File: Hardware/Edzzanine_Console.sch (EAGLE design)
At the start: 37 parts, among them U2 FTS31XS-U, U4 TPS62065

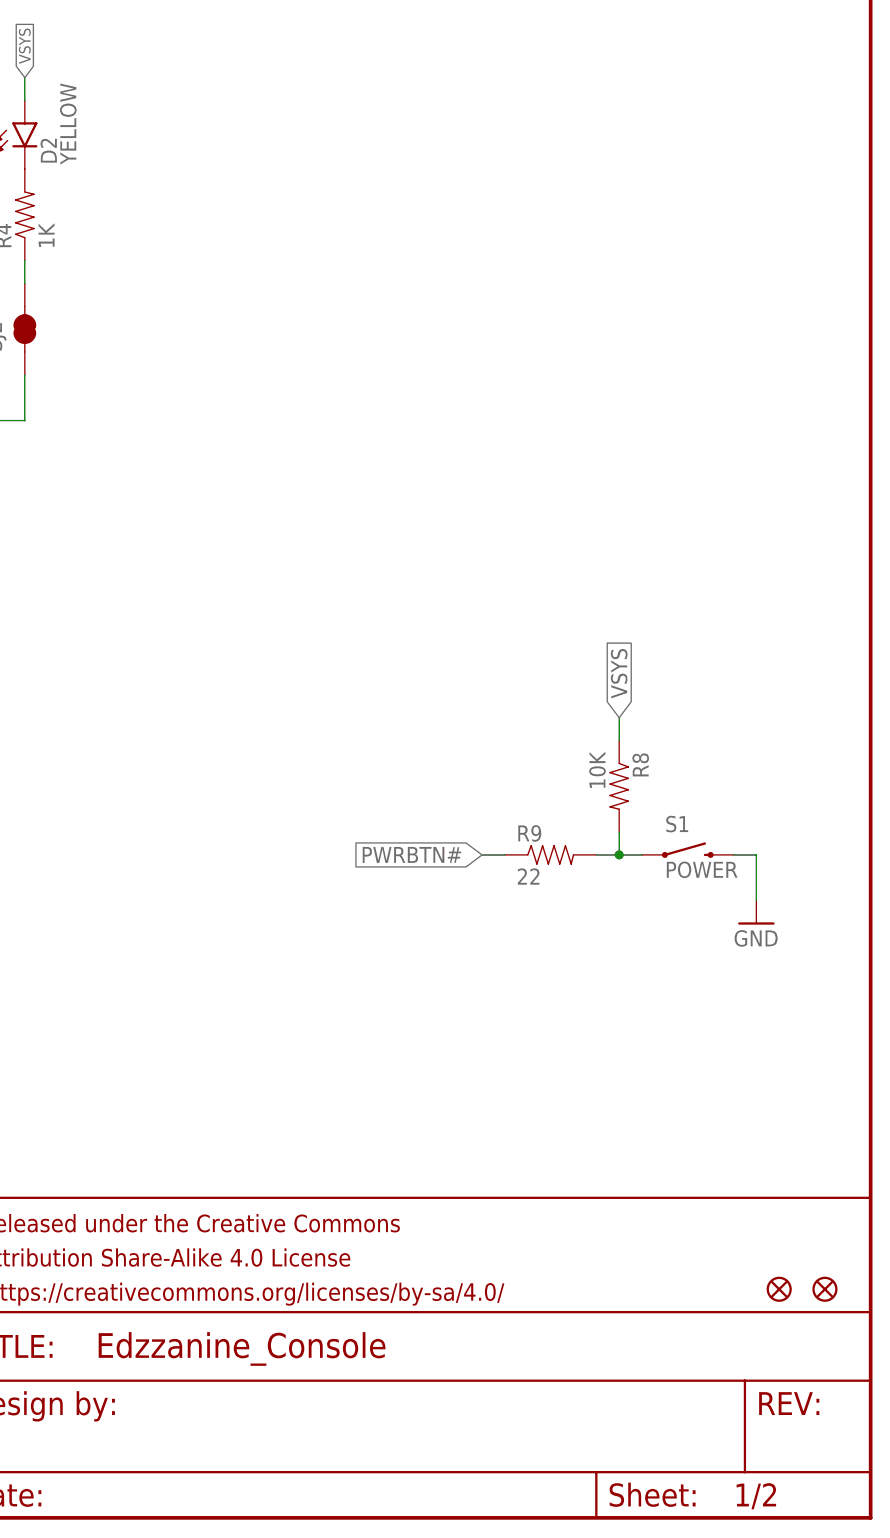
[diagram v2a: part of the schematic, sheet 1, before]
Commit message: Added DCIN enable circuit replaced power button with new side shooting SMD switch Fixed dimensions corrected ground planes to not include orphans corrected name of board added DCIN pin
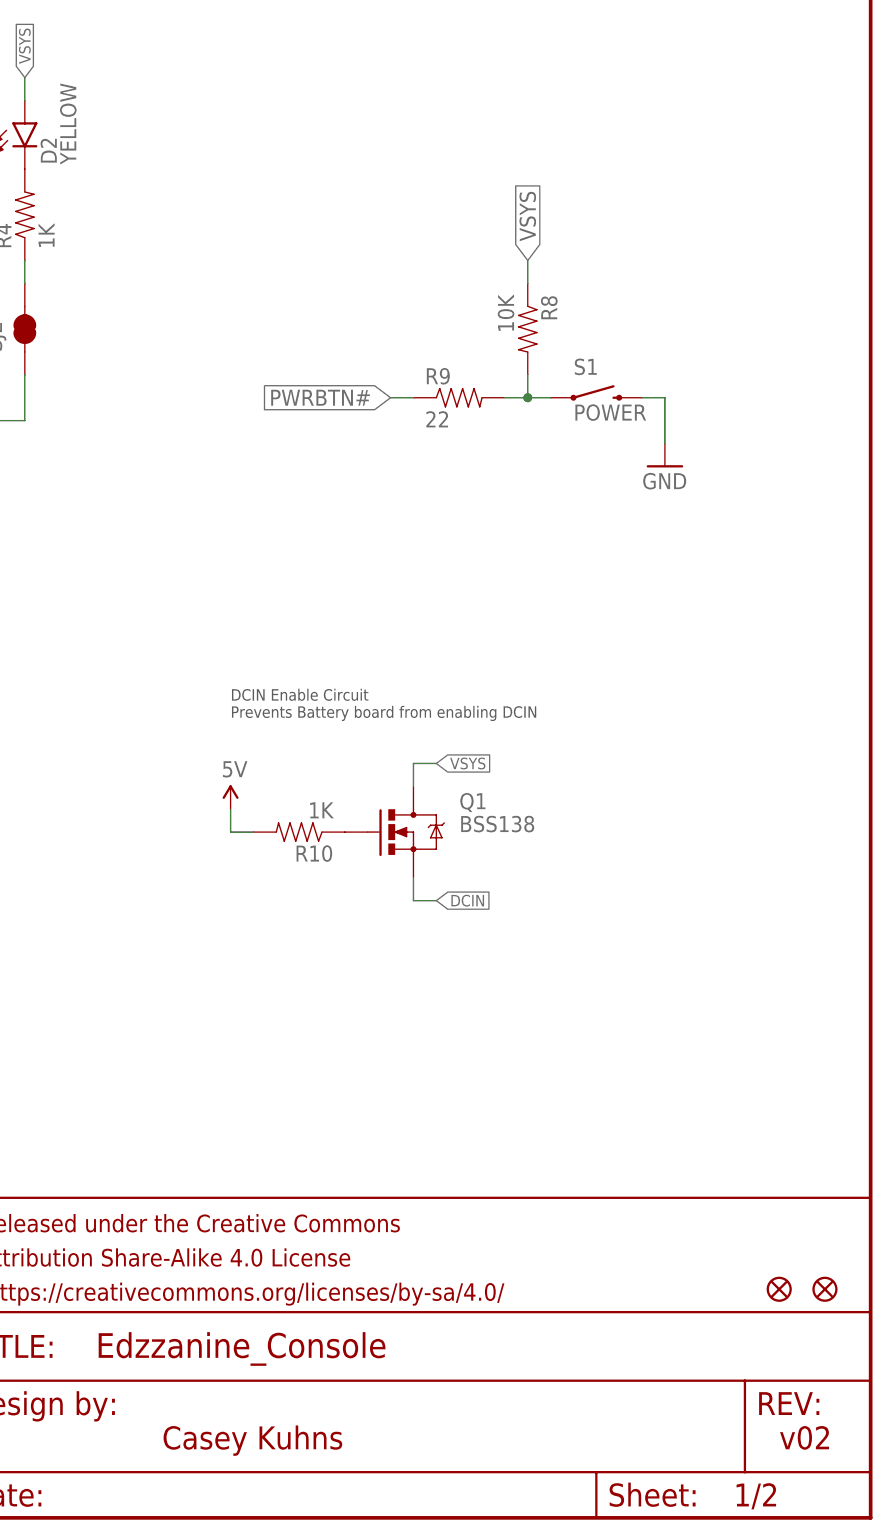
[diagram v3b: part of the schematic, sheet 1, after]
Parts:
- added Q1: BSS138, SparkFun-DiscreteSemi:MOSFET-NCHANNELBSS138
- added R10: 1K, SparkFun-Resistors:1KOHM1/10W1%(0603)
- S1: device SparkFun-Electromechanical:SWITCH-MOMENTARY-2-SMD-1101NE -> SparkFun-Electromechanical:SWITCH-MOMENTARY-2TACTILE-SWITCH-SMD-RIGHT-ANGLE
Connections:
- new net DCIN: E1.DCIN, Q1.S, U$3.DCIN
- new net N$16: Q1.G, R10.1
- net 5V: now also R10.2
- net VSYS: now also Q1.D
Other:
- note added: "Casey Kuhns"
- note added: "DCIN Enable Circuit Prevents Battery board from enabling DCIN"
- note added: "v02"
- moved on the sheet: R8, R9, S1
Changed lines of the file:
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@@
 <part name="R6" library="SparkFun-Resistors" deviceset="100OHM1/10W1%(0603)" device="" value="100"/>
 <part name="R7" library="SparkFun-Resistors" deviceset="100OHM1/10W1%(0603)" device="" value="100"/>
-<part name="S1" library="SparkFun-Electromechanical" deviceset="SWITCH-MOMENTARY-2" device="-SMD-1101NE" value="POWER"/>
+<part name="S1" library="SparkFun-Electromechanical" deviceset="SWITCH-MOMENTARY-2" device="TACTILE-SWITCH-SMD-RIGHT-ANGLE" value="POWER"/>
 <part name="R8" library="SparkFun-Resistors" deviceset="10KOHM1/10W1%(0603)" device="0603" value="10K"/>
 <part name="R9" library="SparkFun-Resistors" deviceset="22OHM1/10W1%(0603)" device="" value="22"/>
@@
 <part name="FID1" library="SparkFun-Aesthetics" deviceset="FIDUCIAL" device="1X2"/>
 <part name="FID2" library="SparkFun-Aesthetics" deviceset="FIDUCIAL" device="1X2"/>
+<part name="Q1" library="SparkFun-DiscreteSemi" deviceset="MOSFET-NCHANNEL" device="BSS138" value="BSS138"/>
+<part name="R10" library="SparkFun-Resistors" deviceset="1KOHM1/10W1%(0603)" device="" value="1K"/>
+<part name="SUPPLY7" library="SparkFun-Aesthetics" deviceset="5V" device=""/>
 </parts>
 <sheets>
 <sheet>
 <plain>
+<text x="238.76" y="7.62" size="2.54" layer="94">v02</text>
+<text x="170.18" y="7.62" size="2.54" layer="94">Casey Kuhns</text>
+<text x="177.8" y="88.9" size="1.27" layer="97">DCIN Enable Circuit
+Prevents Battery board from enabling DCIN</text>
 </plain>
 <instances>
@@
 <attribute name="VALUE" x="107.95" y="144.018" size="1.778" layer="96"/>
 </instance>
-<instance part="S1" gate="G$1" x="228.6" y="73.66"/>
-<instance part="R8" gate="G$1" x="220.98" y="81.28" rot="R270"/>
-<instance part="R9" gate="G$1" x="213.36" y="73.66"/>
-<instance part="GND15" gate="1" x="236.22" y="66.04"/>
+<instance part="S1" gate="G$1" x="218.44" y="124.46"/>
+<instance part="R8" gate="G$1" x="210.82" y="132.08" rot="R270"/>
+<instance part="R9" gate="G$1" x="203.2" y="124.46"/>
+<instance part="GND15" gate="1" x="226.06" y="116.84"/>
 <instance part="GND16" gate="1" x="27.94" y="71.12"/>
 <instance part="C8" gate="G$1" x="101.6" y="71.12"/>
@@
 <instance part="FID1" gate="G$1" x="243.84" y="25.4"/>
 <instance part="FID2" gate="G$1" x="238.76" y="25.4"/>
+<instance part="Q1" gate="G$1" x="198.12" y="76.2"/>
+<instance part="R10" gate="G$1" x="185.42" y="76.2" rot="R180"/>
+<instance part="SUPPLY7" gate="G$1" x="177.8" y="78.74"/>
 </instances>
 <busses>
@@
 <segment>
 <pinref part="S1" gate="G$1" pin="2"/>
-<wire x1="233.68" y1="73.66" x2="236.22" y2="73.66" width="0.1524" layer="91"/>
-<wire x1="236.22" y1="73.66" x2="236.22" y2="68.58" width="0.1524" layer="91"/>
+<wire x1="223.52" y1="124.46" x2="226.06" y2="124.46" width="0.1524" layer="91"/>
+<wire x1="226.06" y1="124.46" x2="226.06" y2="119.38" width="0.1524" layer="91"/>
 <pinref part="GND15" gate="1" pin="GND"/>
 </segment>
@@
 <pinref part="SUPPLY11" gate="G$1" pin="5V"/>
 <pinref part="C10" gate="G$1" pin="1"/>
+</segment>
+<segment>
+<pinref part="SUPPLY7" gate="G$1" pin="5V"/>
+<pinref part="R10" gate="G$1" pin="2"/>
+<wire x1="177.8" y1="78.74" x2="177.8" y2="76.2" width="0.1524" layer="91"/>
+<wire x1="177.8" y1="76.2" x2="180.34" y2="76.2" width="0.1524" layer="91"/>
 </segment>
 </net>
@@
 </segment>
 <segment>
-<wire x1="220.98" y1="86.36" x2="220.98" y2="88.9" width="0.1524" layer="91"/>
+<wire x1="210.82" y1="137.16" x2="210.82" y2="139.7" width="0.1524" layer="91"/>
 <pinref part="R8" gate="G$1" pin="1"/>
-<label x="220.98" y="88.9" size="1.778" layer="95" rot="R90" xref="yes"/>
+<label x="210.82" y="139.7" size="1.778" layer="95" rot="R90" xref="yes"/>
+</segment>
+<segment>
+<pinref part="Q1" gate="G$1" pin="D"/>
+<wire x1="198.12" y1="81.28" x2="198.12" y2="83.82" width="0.1524" layer="91"/>
+<wire x1="198.12" y1="83.82" x2="200.66" y2="83.82" width="0.1524" layer="91"/>
+<label x="200.66" y="83.82" size="1.27" layer="95" xref="yes"/>
 </segment>
 </net>
@@
 <pinref part="R9" gate="G$1" pin="2"/>
 <pinref part="R8" gate="G$1" pin="2"/>
-<wire x1="218.44" y1="73.66" x2="220.98" y2="73.66" width="0.1524" layer="91"/>
-<wire x1="220.98" y1="73.66" x2="220.98" y2="76.2" width="0.1524" layer="91"/>
+<wire x1="208.28" y1="124.46" x2="210.82" y2="124.46" width="0.1524" layer="91"/>
+<wire x1="210.82" y1="124.46" x2="210.82" y2="127" width="0.1524" layer="91"/>
 <pinref part="S1" gate="G$1" pin="1"/>
-<wire x1="220.98" y1="73.66" x2="223.52" y2="73.66" width="0.1524" layer="91"/>
-<junction x="220.98" y="73.66"/>
+<wire x1="210.82" y1="124.46" x2="213.36" y2="124.46" width="0.1524" layer="91"/>
+<junction x="210.82" y="124.46"/>
 </segment>
 </net>
@@
 <segment>
 <pinref part="R9" gate="G$1" pin="1"/>
-<wire x1="208.28" y1="73.66" x2="205.74" y2="73.66" width="0.1524" layer="91"/>
-<label x="205.74" y="73.66" size="1.778" layer="95" rot="R180" xref="yes"/>
+<wire x1="198.12" y1="124.46" x2="195.58" y2="124.46" width="0.1524" layer="91"/>
+<label x="195.58" y="124.46" size="1.778" layer="95" rot="R180" xref="yes"/>
 </segment>
 </net>
@@
 <pinref part="L1" gate="G$1" pin="1"/>
 <wire x1="66.04" y1="91.44" x2="63.5" y2="91.44" width="0.1524" layer="91"/>
+</segment>
+</net>
+<net name="DCIN" class="0">
+<segment>
+<wire x1="198.12" y1="68.58" x2="200.66" y2="68.58" width="0.1524" layer="91"/>
+<label x="200.66" y="68.58" size="1.27" layer="95" xref="yes"/>
+<pinref part="Q1" gate="G$1" pin="S"/>
+<wire x1="198.12" y1="68.58" x2="198.12" y2="71.12" width="0.1524" layer="91"/>
+</segment>
+</net>
+<net name="N$16" class="0">
+<segment>
+<pinref part="Q1" gate="G$1" pin="G"/>
+<pinref part="R10" gate="G$1" pin="1"/>
 </segment>
 </net>
@@
 </segment>
 </net>
+<net name="DCIN" class="0">
+<segment>
+<pinref part="E1" gate="G$1" pin="DCIN"/>
+<wire x1="25.4" y1="152.4" x2="22.86" y2="152.4" width="0.1524" layer="91"/>
+<label x="22.86" y="152.4" size="1.27" layer="95" rot="R180" xref="yes"/>
+</segment>
+<segment>
+<pinref part="U$3" gate="G$1" pin="DCIN"/>
+<wire x1="172.72" y1="152.4" x2="170.18" y2="152.4" width="0.1524" layer="91"/>
+<label x="170.18" y="152.4" size="1.27" layer="95" rot="R180" xref="yes"/>
+</segment>
+</net>
 </nets>
 </sheet>
@@
 </schematic>
 </drawing>
+<compatibility>
+<note version="6.3" minversion="6.2.2" severity="warning">
+Since Version 6.2.2 text objects can contain more than one line,
+which will not be processed correctly with this version.
+</note>
+</compatibility>
 </eagle>
